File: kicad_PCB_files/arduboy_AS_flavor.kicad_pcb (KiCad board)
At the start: 2 copper layers, 2 parts, among them U1 ATmega32U4-AU, U2 ATmega32U4-MU

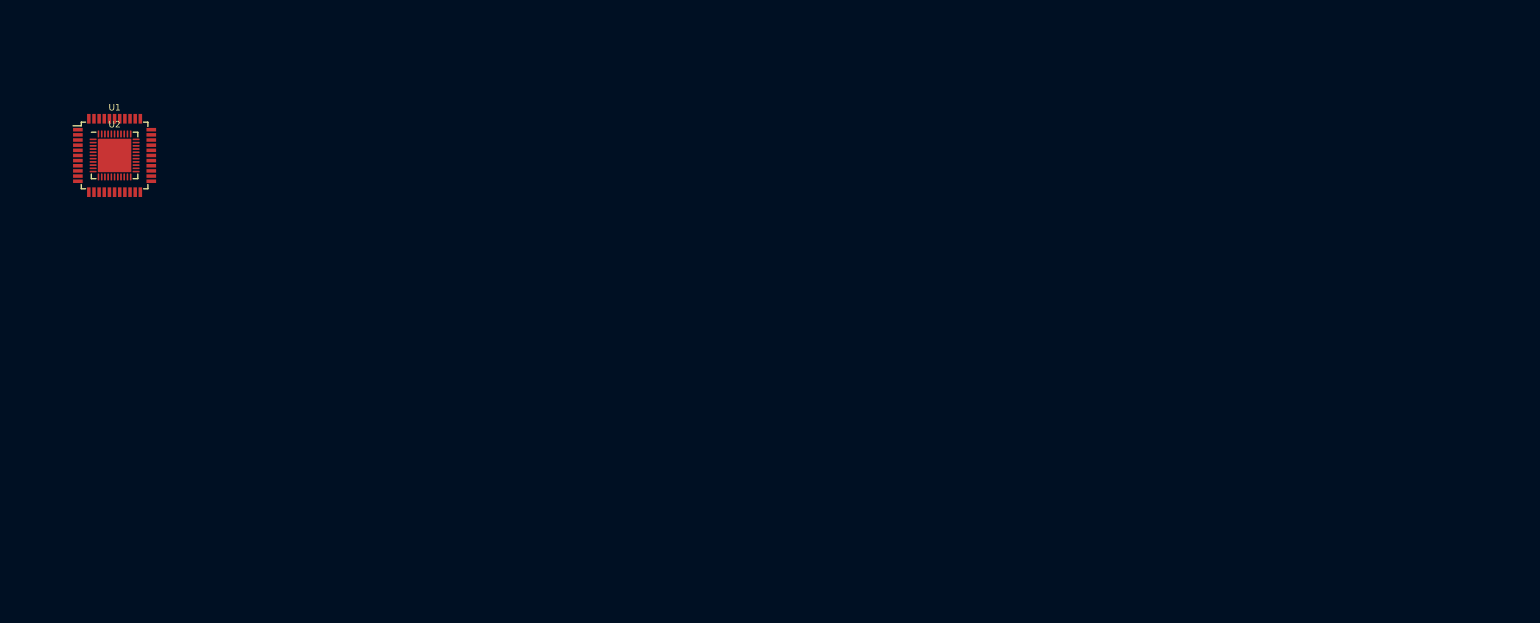
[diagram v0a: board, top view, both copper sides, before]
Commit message: Changed screen capacitor's size and value PCB mockup added
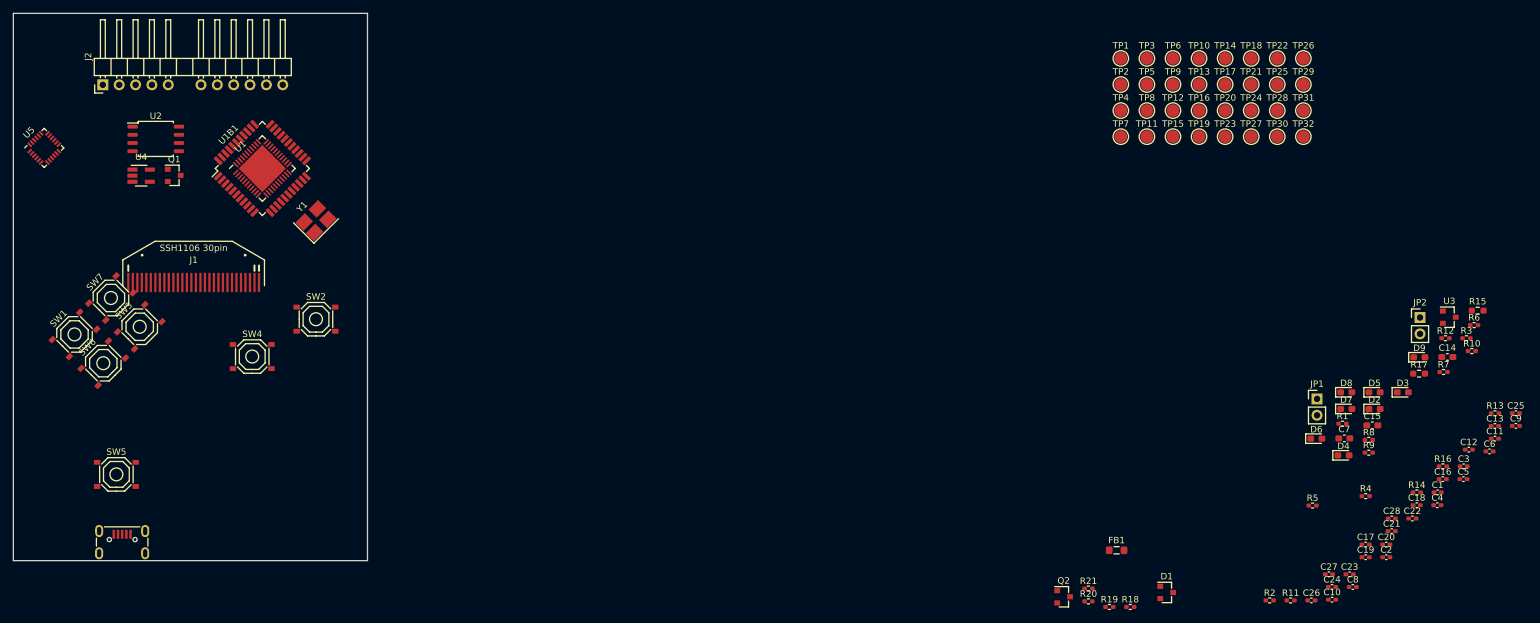
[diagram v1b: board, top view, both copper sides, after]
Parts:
- added C1: 100nF, Capacitor_SMD:C_0402_1005Metric_Pad0.74x0.62mm_HandSolder, F.Cu at (251.2, 104.4)
- added C10: 1uF, Capacitor_SMD:C_0402_1005Metric_Pad0.74x0.62mm_HandSolder, F.Cu at (234.8, 121.1)
- added C11: 1uF, Capacitor_SMD:C_0402_1005Metric_Pad0.74x0.62mm_HandSolder, F.Cu at (260.1, 96.1)
- added C12: 1uF, Capacitor_SMD:C_0402_1005Metric_Pad0.74x0.62mm_HandSolder, F.Cu at (256.1, 97.8)
- added C13: 1uF, Capacitor_SMD:C_0402_1005Metric_Pad0.74x0.62mm_HandSolder, F.Cu at (260.1, 94.1)
- added C14: 2.2uF, Capacitor_SMD:C_0603_1608Metric_Pad1.08x0.95mm_HandSolder, F.Cu at (252.7, 83.4)
- added C15: 2.2uF, Capacitor_SMD:C_0603_1608Metric_Pad1.08x0.95mm_HandSolder, F.Cu at (241.1, 94.0)
- added C16: 100nF, Capacitor_SMD:C_0402_1005Metric_Pad0.74x0.62mm_HandSolder, F.Cu at (252.0, 102.3)
- added C17: 100nF, Capacitor_SMD:C_0402_1005Metric_Pad0.74x0.62mm_HandSolder, F.Cu at (240.0, 112.5)
- added C18: 100nF, Capacitor_SMD:C_0402_1005Metric_Pad0.74x0.62mm_HandSolder, F.Cu at (247.9, 106.4)
- added C19: 100nF, Capacitor_SMD:C_0402_1005Metric_Pad0.74x0.62mm_HandSolder, F.Cu at (240.0, 114.5)
- added C2: 12pF, Capacitor_SMD:C_0402_1005Metric_Pad0.74x0.62mm_HandSolder, F.Cu at (243.2, 114.5)
- added C20: 100nF, Capacitor_SMD:C_0402_1005Metric_Pad0.74x0.62mm_HandSolder, F.Cu at (243.2, 112.5)
- added C21: 100nF, Capacitor_SMD:C_0402_1005Metric_Pad0.74x0.62mm_HandSolder, F.Cu at (244.1, 110.4)
- added C22: 100nF, Capacitor_SMD:C_0402_1005Metric_Pad0.74x0.62mm_HandSolder, F.Cu at (247.3, 108.5)
- added C23: 10nF, Capacitor_SMD:C_0402_1005Metric_Pad0.74x0.62mm_HandSolder, F.Cu at (237.5, 117.1)
- added C24: 100nF, Capacitor_SMD:C_0402_1005Metric_Pad0.74x0.62mm_HandSolder, F.Cu at (234.8, 119.1)
- added C25: 2.2nF, Capacitor_SMD:C_0402_1005Metric_Pad0.74x0.62mm_HandSolder, F.Cu at (263.4, 92.1)
- added C26: 100nF, Capacitor_SMD:C_0402_1005Metric_Pad0.74x0.62mm_HandSolder, F.Cu at (231.6, 121.2)
- added C27: 1uF, Capacitor_SMD:C_0402_1005Metric_Pad0.74x0.62mm_HandSolder, F.Cu at (234.3, 117.1)
- added C28: 1uF, Capacitor_SMD:C_0402_1005Metric_Pad0.74x0.62mm_HandSolder, F.Cu at (244.1, 108.5)
- added C3: 12pF, Capacitor_SMD:C_0402_1005Metric_Pad0.74x0.62mm_HandSolder, F.Cu at (255.2, 100.3)
- added C4: 100nF, Capacitor_SMD:C_0402_1005Metric_Pad0.74x0.62mm_HandSolder, F.Cu at (251.2, 106.4)
- added C5: 1uF, Capacitor_SMD:C_0402_1005Metric_Pad0.74x0.62mm_HandSolder, F.Cu at (255.2, 102.3)
- added C6: 1uF, Capacitor_SMD:C_0402_1005Metric_Pad0.74x0.62mm_HandSolder, F.Cu at (259.3, 98.0)
- added C7: 10uF, Capacitor_SMD:C_0603_1608Metric_Pad1.08x0.95mm_HandSolder, F.Cu at (236.7, 96.0)
- added C8: 1uF, Capacitor_SMD:C_0402_1005Metric_Pad0.74x0.62mm_HandSolder, F.Cu at (238.0, 119.1)
- added C9: 1uF, Capacitor_SMD:C_0402_1005Metric_Pad0.74x0.62mm_HandSolder, F.Cu at (263.4, 94.1)
- added D1: BAV70, Package_TO_SOT_SMD:SOT-23, F.Cu at (209.1, 119.9)
- added D2: Red, LED_SMD:LED_0603_1608Metric_Pad1.05x0.95mm_HandSolder, F.Cu at (241.4, 91.4)
- added D3: Green, LED_SMD:LED_0603_1608Metric_Pad1.05x0.95mm_HandSolder, F.Cu at (245.8, 88.8)
- added D4: Blue, LED_SMD:LED_0603_1608Metric_Pad1.05x0.95mm_HandSolder, F.Cu at (236.6, 98.6)
- added D5: Yellow, LED_SMD:LED_0603_1608Metric_Pad1.05x0.95mm_HandSolder, F.Cu at (241.4, 88.8)
- added D6: Yellow, LED_SMD:LED_0603_1608Metric_Pad1.05x0.95mm_HandSolder, F.Cu at (232.4, 96.0)
- added D7: Yellow, LED_SMD:LED_0603_1608Metric_Pad1.05x0.95mm_HandSolder, F.Cu at (237.0, 91.4)
- added D8: Yellow, LED_SMD:LED_0603_1608Metric_Pad1.05x0.95mm_HandSolder, F.Cu at (237.0, 88.8)
- added D9: Yellow, LED_SMD:LED_0603_1608Metric_Pad1.05x0.95mm_HandSolder, F.Cu at (248.4, 83.4)
- added FB1: 100R @ 100MHz, Inductor_SMD:L_0805_2012Metric_Pad1.05x1.20mm_HandSolder, F.Cu at (201.3, 113.4)
- added J1: SSD1306_SSH1106, arduboy:SSH1106_30pin_P0.7mm, F.Cu at (58.0, 72.3)
- added J2: Expansion_port_NEW, arduboy:PinHeader_1x12_P2.54mm_SLOTTED_ROTATED, F.Cu at (43.9, 41.1)
- added J3: USB_B_Micro, arduboy:USB_MICRO_B_C456008, F.Cu at (46.9, 115.0)
- added JP1: Speaker, Connector_PinHeader_2.54mm:PinHeader_1x02_P2.54mm_Vertical, F.Cu at (232.5, 89.9)
- added JP2: LiPo, Connector_PinHeader_2.54mm:PinHeader_1x02_P2.54mm_Vertical, F.Cu at (248.5, 77.2)
- added Q1: 2N7002, Package_TO_SOT_SMD:SOT-23, F.Cu at (55.0, 55.2)
- added Q2: Si2301CDS, Package_TO_SOT_SMD:SOT-23, F.Cu at (193.1, 120.6)
- added R1: 10k, Resistor_SMD:R_0402_1005Metric_Pad0.72x0.64mm_HandSolder, F.Cu at (236.4, 93.7)
- added R10: 680, Resistor_SMD:R_0402_1005Metric_Pad0.72x0.64mm_HandSolder, F.Cu at (256.5, 82.5)
- added R11: 680, Resistor_SMD:R_0402_1005Metric_Pad0.72x0.64mm_HandSolder, F.Cu at (228.4, 121.2)
- added R12: 6.8k, Resistor_SMD:R_0402_1005Metric_Pad0.72x0.64mm_HandSolder, F.Cu at (252.4, 80.5)
- added R13: 3.3k, Resistor_SMD:R_0402_1005Metric_Pad0.72x0.64mm_HandSolder, F.Cu at (260.1, 92.1)
- added R14: 3.3k, Resistor_SMD:R_0402_1005Metric_Pad0.72x0.64mm_HandSolder, F.Cu at (248.0, 104.4)
- added R15: 220, Resistor_SMD:R_0603_1608Metric_Pad0.98x0.95mm_HandSolder, F.Cu at (257.4, 76.2)
- added R16: 4.7k, Resistor_SMD:R_0402_1005Metric_Pad0.72x0.64mm_HandSolder, F.Cu at (252.0, 100.4)
- added R17: 390k, Resistor_SMD:R_0603_1608Metric_Pad0.98x0.95mm_HandSolder, F.Cu at (248.3, 86.0)
- added R18: 4.7k, Resistor_SMD:R_0402_1005Metric_Pad0.72x0.64mm_HandSolder, F.Cu at (203.5, 122.2)
- added R19: 4.7k, Resistor_SMD:R_0402_1005Metric_Pad0.72x0.64mm_HandSolder, F.Cu at (200.2, 122.2)
- added R2: 10k, Resistor_SMD:R_0402_1005Metric_Pad0.72x0.64mm_HandSolder, F.Cu at (225.1, 121.2)
- added R20: 22, Resistor_SMD:R_0402_1005Metric_Pad0.72x0.64mm_HandSolder, F.Cu at (197.0, 121.3)
- added R21: 22, Resistor_SMD:R_0402_1005Metric_Pad0.72x0.64mm_HandSolder, F.Cu at (197.0, 119.3)
- added R3: 10k, Resistor_SMD:R_0402_1005Metric_Pad0.72x0.64mm_HandSolder, F.Cu at (255.7, 80.5)
- added R4: 10k, Resistor_SMD:R_0402_1005Metric_Pad0.72x0.64mm_HandSolder, F.Cu at (240.0, 105.0)
- added R5: 10k, Resistor_SMD:R_0402_1005Metric_Pad0.72x0.64mm_HandSolder, F.Cu at (231.8, 106.4)
- added R6: 6.8k, Resistor_SMD:R_0402_1005Metric_Pad0.72x0.64mm_HandSolder, F.Cu at (256.9, 78.4)
- added R7: 3.3k, Resistor_SMD:R_0402_1005Metric_Pad0.72x0.64mm_HandSolder, F.Cu at (252.1, 85.7)
- added R8: 10k, Resistor_SMD:R_0402_1005Metric_Pad0.72x0.64mm_HandSolder, F.Cu at (240.5, 96.2)
- added R9: 1.2k, Resistor_SMD:R_0402_1005Metric_Pad0.72x0.64mm_HandSolder, F.Cu at (240.5, 98.2)
- added SW1: RST Button, arduboy:button_TS-1187A-B-A-B, F.Cu at (39.5, 79.9)
- added SW2: UP Button, arduboy:button_TS-1187A-B-A-B, F.Cu at (77.0, 77.5)
- added SW3: DOWN Button, arduboy:button_TS-1187A-B-A-B, F.Cu at (49.6, 78.7)
- added SW4: LEFT Button, arduboy:button_TS-1187A-B-A-B, F.Cu at (67.1, 83.3)
- added SW5: RIGHT Button, arduboy:button_TS-1187A-B-A-B, F.Cu at (46.0, 101.6)
- added SW6: RIGHT Button, arduboy:button_TS-1187A-B-A-B, F.Cu at (44.0, 84.3)
- added SW7: RIGHT Button, arduboy:button_TS-1187A-B-A-B, F.Cu at (45.2, 74.2)
- added TP1: GYRO_INT, TestPoint:TestPoint_Pad_D2.0mm, F.Cu at (202.0, 37.0)
- added TP10: D4/D4/~OLED_DC, TestPoint:TestPoint_Pad_D2.0mm, F.Cu at (214.2, 37.0)
- added TP11: D14/PB3/MISO, TestPoint:TestPoint_Pad_D2.0mm, F.Cu at (206.1, 49.1)
- added TP12: D6/D7/~OLED_RST, TestPoint:TestPoint_Pad_D2.0mm, F.Cu at (210.1, 45.1)
- added TP13: D16/PB2/MOSI, TestPoint:TestPoint_Pad_D2.0mm, F.Cu at (214.2, 41.0)
- added TP14: D12/D6/~OLED_CS, TestPoint:TestPoint_Pad_D2.0mm, F.Cu at (218.2, 37.0)
- added TP15: D15/PB1/SCK, TestPoint:TestPoint_Pad_D2.0mm, F.Cu at (210.1, 49.1)
- added TP16: USB_ID, TestPoint:TestPoint_Pad_D2.0mm, F.Cu at (214.2, 45.1)
- added TP17: D7/E6/A, TestPoint:TestPoint_Pad_D2.0mm, F.Cu at (218.2, 41.0)
- added TP18: A4/F1/EN, TestPoint:TestPoint_Pad_D2.0mm, F.Cu at (222.2, 37.0)
- added TP19: D8/PB4/B, TestPoint:TestPoint_Pad_D2.0mm, F.Cu at (214.2, 49.1)
- added TP2: D2/PD1/SDA+FLASH_CS, TestPoint:TestPoint_Pad_D2.0mm, F.Cu at (202.0, 41.0)
- added TP20: A5/F0, TestPoint:TestPoint_Pad_D2.0mm, F.Cu at (218.2, 45.1)
- added TP21: A0/PF7/UP, TestPoint:TestPoint_Pad_D2.0mm, F.Cu at (222.2, 41.0)
- added TP22: D1/PD3/TX, TestPoint:TestPoint_Pad_D2.0mm, F.Cu at (226.3, 37.0)
- added TP23: A1/F6/RIGHT, TestPoint:TestPoint_Pad_D2.0mm, F.Cu at (218.2, 49.1)
- added TP24: D0/PD2/RX, TestPoint:TestPoint_Pad_D2.0mm, F.Cu at (222.2, 45.1)
- added TP25: A2/F5/LEFT, TestPoint:TestPoint_Pad_D2.0mm, F.Cu at (226.3, 41.0)
- added TP26: D13/PC7/SPKR2, TestPoint:TestPoint_Pad_D2.0mm, F.Cu at (230.3, 37.0)
- added TP27: A3/F4/DOWN, TestPoint:TestPoint_Pad_D2.0mm, F.Cu at (222.2, 49.1)
- added TP28: D5/PC6/SPKR1, TestPoint:TestPoint_Pad_D2.0mm, F.Cu at (226.3, 45.1)
- added TP29: 3V3, TestPoint:TestPoint_Pad_D2.0mm, F.Cu at (230.3, 41.0)
- added TP3: ~RST, TestPoint:TestPoint_Pad_D2.0mm, F.Cu at (206.1, 37.0)
- added TP30: VCC, TestPoint:TestPoint_Pad_D2.0mm, F.Cu at (226.3, 49.1)
- added TP31: 5V_USB, TestPoint:TestPoint_Pad_D2.0mm, F.Cu at (230.3, 45.1)
- added TP32: GND, TestPoint:TestPoint_Pad_D2.0mm, F.Cu at (230.3, 49.1)
- added TP4: D3/PD0/SCL, TestPoint:TestPoint_Pad_D2.0mm, F.Cu at (202.0, 45.1)
- added TP5: D11/PB7/~LED_G, TestPoint:TestPoint_Pad_D2.0mm, F.Cu at (206.1, 41.0)
- added TP6: D17/PB0/~RX_LED, TestPoint:TestPoint_Pad_D2.0mm, F.Cu at (210.1, 37.0)
- added TP7: D10/PB6/~LED_R, TestPoint:TestPoint_Pad_D2.0mm, F.Cu at (202.0, 49.1)
- added TP8: D30/D5/~TX_LED, TestPoint:TestPoint_Pad_D2.0mm, F.Cu at (206.1, 45.1)
- added TP9: D9/PB5/~LED_B, TestPoint:TestPoint_Pad_D2.0mm, F.Cu at (210.1, 41.0)
- added U2: W25Q128JVSIQ, Package_SO:SOIC-8_5.23x5.23mm_P1.27mm, F.Cu at (52.1, 49.5)
- added U3: XC6206P33, Package_TO_SOT_SMD:SOT-23, F.Cu at (253.0, 77.2)
- added U4: TP4054, Package_TO_SOT_SMD:SOT-23-5_HandSoldering, F.Cu at (49.9, 55.2)
- added U5: MPU-6050, Sensor_Motion:InvenSense_QFN-24_4x4mm_P0.5mm, F.Cu at (34.8, 50.9)
- added Y1: 16MHz, Crystal:Crystal_SMD_3225-4Pin_3.2x2.5mm_HandSoldering, F.Cu at (77.0, 62.2)
- moved U1 23.0 mm to (68.7, 54.1), turned to 45 degrees
- moved U1B1 23.0 mm to (68.7, 54.1), turned to 45 degrees
- renumbered U2 to U1, U1 to U1B1
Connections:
- net Net-(U1-Pad1) renamed Btn_A
- net Net-(U1-Pad10) renamed MOSI
- net Net-(U1-Pad11) renamed MISO
- net Net-(U1-Pad12) renamed LED_G
- net Net-(U1-Pad13) renamed RST
- net Net-(U1-Pad16) renamed XTAL2
- net Net-(U1-Pad17) renamed XTAL1
- net Net-(U1-Pad18) renamed SCL_3V3
- net Net-(U1-Pad19) renamed SDA+FCS
- net Net-(U1-Pad20) renamed RX
- net Net-(U1-Pad21) renamed TX
- net Net-(U1-Pad22) renamed TX_LED
- net Net-(U1-Pad25) renamed OLED_DC
- net Net-(U1-Pad26) renamed OLED_CS
- net Net-(U1-Pad27) renamed OLED_RST
- net Net-(U1-Pad28) renamed Btn_B
- net Net-(U1-Pad29) renamed LED_B
- net Net-(U1-Pad3) renamed D-
- net Net-(U1-Pad30) renamed LED_R
- net Net-(U1-Pad31) renamed SPKR1
- net Net-(U1-Pad32) renamed SPKR2
- net Net-(U1-Pad36) renamed Btn_UP
- net Net-(U1-Pad37) renamed Btn_RIGHT
- net Net-(U1-Pad38) renamed Btn_LEFT
- net Net-(U1-Pad39) renamed Btn_DOWN
- net Net-(U1-Pad4) renamed D+
- net Net-(U1-Pad40) renamed EN
- net Net-(U1-Pad41) renamed A5
- net Net-(U1-Pad42) renamed AREF
- net Net-(U1-Pad6) renamed UCAP
- net Net-(U1-Pad8) renamed RX_LED
- net Net-(U1-Pad9) renamed SCK
- U1 pad 14: Net-(U1-Pad14) -> VCC
- U1 pad 15: Net-(U1-Pad15) -> GND
- U1 pad 2: Net-(U1-Pad2) -> +5V
- U1 pad 23: Net-(U1-Pad15) -> GND
- U1 pad 24: Net-(U1-Pad24) -> VCC
- U1 pad 33: Net-(U1-Pad33) -> GND
- U1 pad 34: Net-(U1-Pad14) -> VCC
- U1 pad 35: Net-(U1-Pad15) -> GND
- U1 pad 43: Net-(U1-Pad15) -> GND
- U1 pad 44: Net-(U1-Pad24) -> VCC
- U1 pad 45: Net-(U1-Pad15) -> GND
- U1 pad 5: Net-(U1-Pad5) -> GND
- U1 pad 7: Net-(U1-Pad7) -> +5V
- U1B1 pad 14: Net-(U1-Pad14) -> VCC
- U1B1 pad 15: Net-(U1-Pad15) -> GND
- U1B1 pad 2: Net-(U1-Pad2) -> +5V
- U1B1 pad 23: Net-(U1-Pad15) -> GND
- U1B1 pad 24: Net-(U1-Pad24) -> VCC
- U1B1 pad 33: Net-(U1-Pad33) -> GND
- U1B1 pad 34: Net-(U1-Pad14) -> VCC
- U1B1 pad 35: Net-(U1-Pad15) -> GND
- U1B1 pad 43: Net-(U1-Pad15) -> GND
- U1B1 pad 44: Net-(U1-Pad24) -> VCC
- U1B1 pad 5: Net-(U1-Pad5) -> GND
- U1B1 pad 7: Net-(U1-Pad7) -> +5V
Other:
- board outline added: 55 x 85 mm

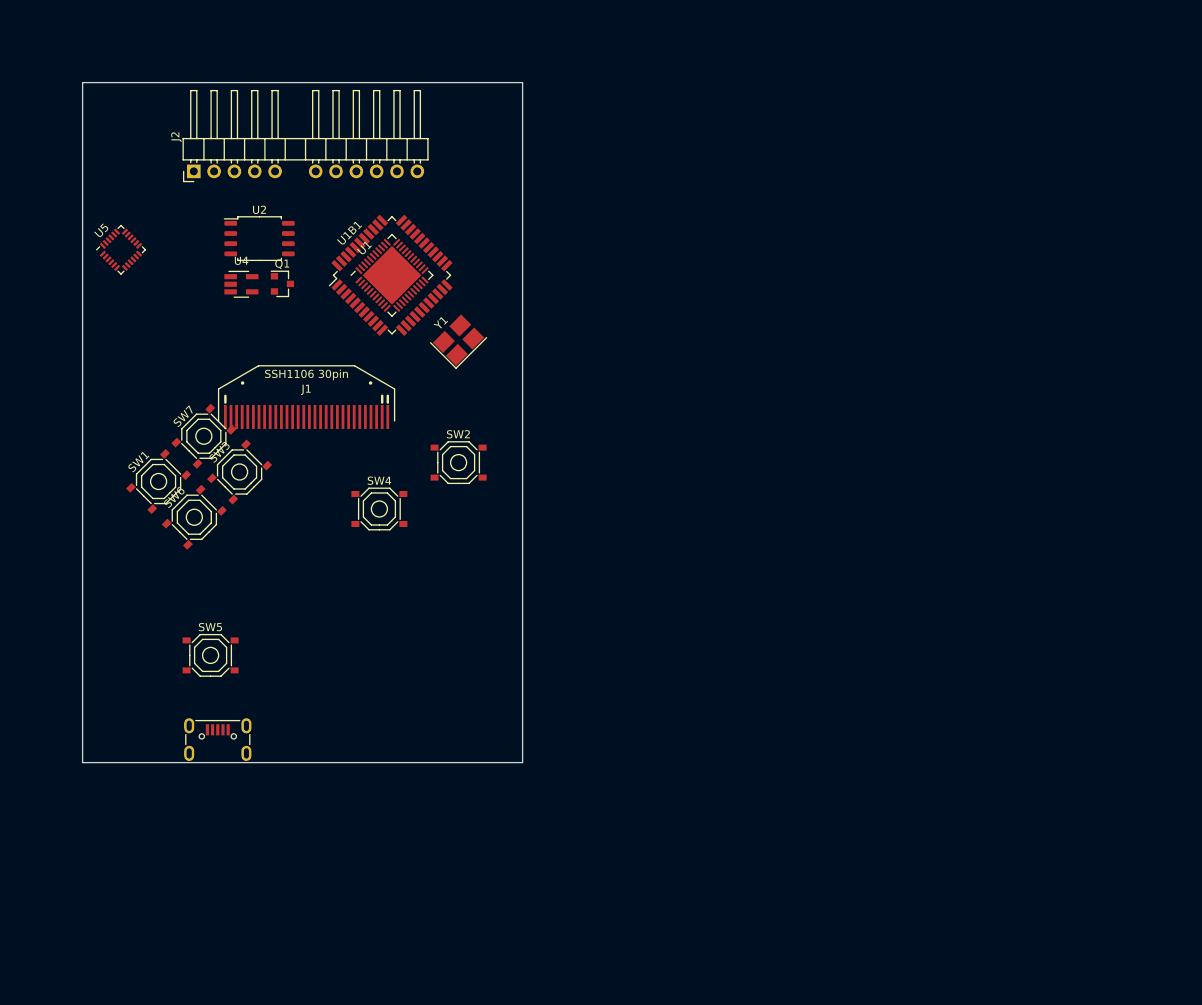
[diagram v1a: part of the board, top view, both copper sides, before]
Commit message: PCB changes - Button footprints for clicky OR silent switches
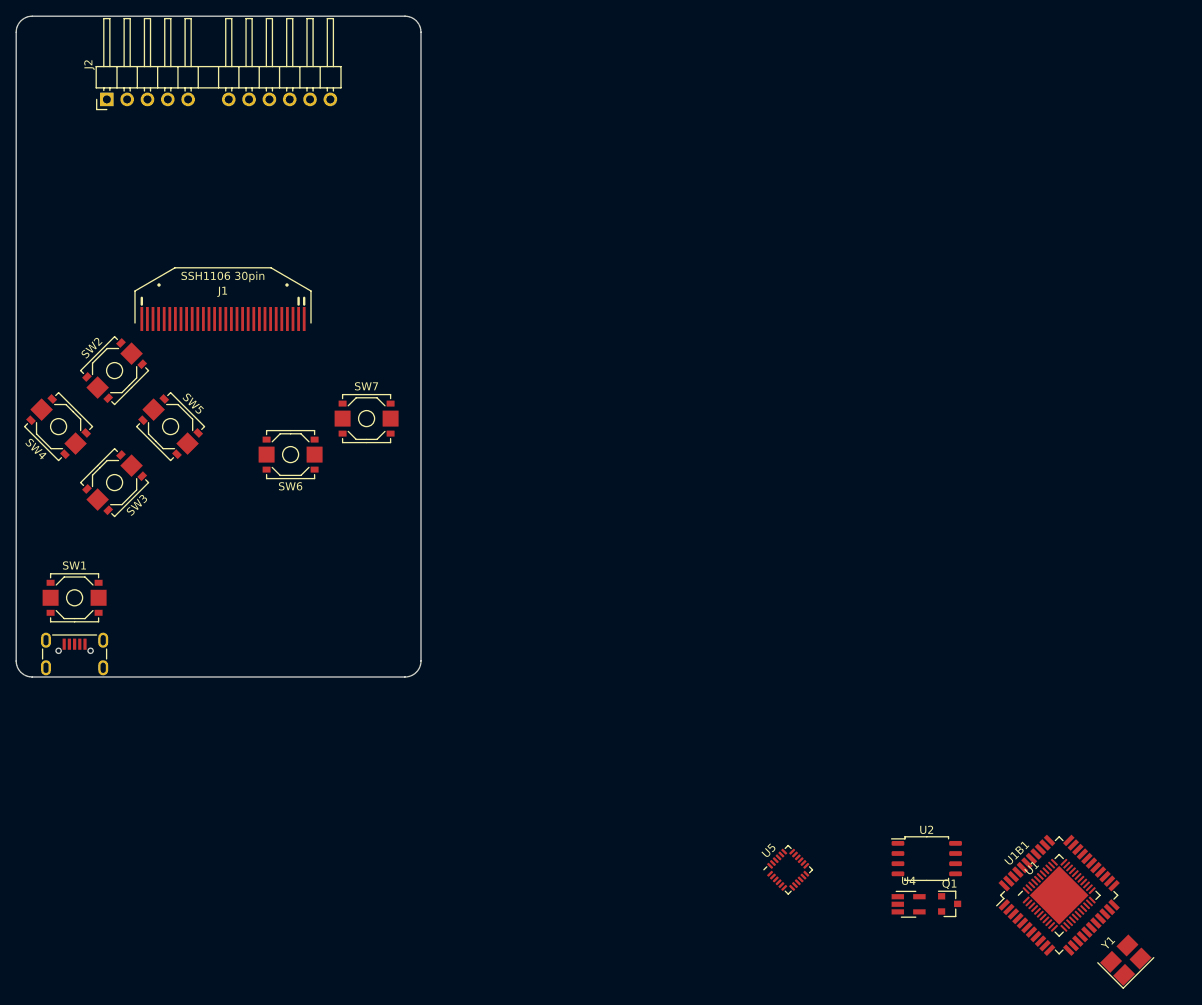
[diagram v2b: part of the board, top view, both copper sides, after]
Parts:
- SW6: value RIGHT Button -> A Button
- SW7: value RIGHT Button -> B Button
- moved Q1 113.8 mm to (138.4, 132.7)
- moved U1 113.8 mm to (152.1, 131.6)
- moved U1B1 113.8 mm to (152.1, 131.6)
- moved U2 113.8 mm to (135.5, 127.0)
- moved U4 113.8 mm to (133.2, 132.7)
- moved U5 113.8 mm to (118.2, 128.4)
- moved Y1 113.8 mm to (160.4, 139.7)
- moved SW2 44.5 mm to (34.0, 66.0), turned to 45 degrees
- moved SW4 41.4 mm to (27.0, 73.0), turned to 135 degrees
- moved SW5 29.0 mm to (41.0, 73.0), turned to 315 degrees
- moved J3 20.9 mm to (29.0, 104.3)
- moved SW7 20.5 mm to (65.5, 72.0), turned to 0 degrees
- moved SW1 17.9 mm to (29.0, 94.4), turned to 0 degrees
- moved J1 16.1 mm to (47.5, 60.0)
- moved SW3 15.7 mm to (34.0, 80.0), turned to 225 degrees
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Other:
- board size 55 x 85 mm -> 50.6 x 82.6 mm
- board text added: "Max unit size (86x54 mm)"
- board text added: "Todo: Add dpad hole"

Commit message: Added mechanical mounting points Continued PCB placement feasibility
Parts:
- added H1: JLC, arduboy:JLCPCB_assembly_hole, F.Cu at (24.0, 102.0)
- added H2: JLC, arduboy:JLCPCB_assembly_hole, F.Cu at (28.5, 23.0)
- added H3: JLC, arduboy:JLCPCB_assembly_hole, F.Cu at (65.5, 23.0)
- added H4: M2, arduboy:M2_mounting_hole, F.Cu at (25.0, 25.0)
- added H5: M2, arduboy:M2_mounting_hole, F.Cu at (69.0, 25.0)
- added H6: M2, arduboy:M2_mounting_hole, F.Cu at (69.0, 83.9)
- added H7: M2, arduboy:M2_mounting_hole, F.Cu at (25.0, 80.8)
- C1, C10, C11, C12, C13, C16, C17, C18, C19, C2, C20, C21, C22, C23, C24, C25, C26, C27, C28, C3, C4, C5, C6, C8, C9: footprint Capacitor_SMD:C_0402_1005Metric_Pad0.74x0.62mm_HandSolder -> no_refdes:0402_HandSolder
- C14, C15, C7: footprint Capacitor_SMD:C_0603_1608Metric_Pad1.08x0.95mm_HandSolder -> no_refdes:0603_HandSolder
- J1: footprint arduboy:SSH1106_30pin_P0.7mm -> arduboy:SSD1306_30pin_P0.7mm
- R1, R10, R11, R12, R13, R14, R16, R18, R19, R2, R20, R21, R3, R4, R5, R6, R7, R8, R9: footprint Resistor_SMD:R_0402_1005Metric_Pad0.72x0.64mm_HandSolder -> no_refdes:0402_HandSolder
- R15, R17: footprint Resistor_SMD:R_0603_1608Metric_Pad0.98x0.95mm_HandSolder -> no_refdes:0603_HandSolder
- TP1, TP10, TP11, TP12, TP13, TP14, TP15, TP16, TP17, TP18, TP19, TP2, TP20, TP21, TP22, TP23, TP24, TP25, TP26, TP27, TP28, TP29, TP3, TP30, TP31, TP32, TP4, TP5, TP6, TP7, TP8, TP9: moved to B.Cu
- Y1: footprint Crystal:Crystal_SMD_3225-4Pin_3.2x2.5mm_HandSoldering -> Crystal:Crystal_SMD_3225-4Pin_3.2x2.5mm
- moved D3 225.9 mm to (25.6, 38.6), turned to 180 degrees
- moved D2 221.8 mm to (25.6, 40.3), turned to 180 degrees
- moved D4 219.8 mm to (25.6, 36.9), turned to 180 degrees
- moved C3 194.9 mm to (65.2, 57.1)
- moved D7 190.9 mm to (46.4, 81.6), turned to 90 degrees
- moved C2 185.5 mm to (65.2, 62.3), turned to 180 degrees
- moved TP10 180.7 mm to (44.5, 99.3)
- moved TP22 180.7 mm to (56.7, 99.3)
- moved TP3 180.7 mm to (36.5, 99.3)
- moved TP1 180.7 mm to (32.4, 99.3)
- moved TP14 180.7 mm to (48.6, 99.3)
- moved TP18 180.7 mm to (52.6, 99.3)
- moved TP26 180.7 mm to (60.8, 99.3)
- moved TP6 180.7 mm to (40.5, 99.3)
- moved TP13 178.0 mm to (44.5, 95.2)
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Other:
- board text added: "Lipo protected 502030"
- board text added: "piezo 15mm"
